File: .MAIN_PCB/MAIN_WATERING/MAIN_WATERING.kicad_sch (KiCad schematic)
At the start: 5 parts, among them J1 Conn_01x04_Pin, SW1 SW_Push, U1 XIAO-ESP32-C3-SMD

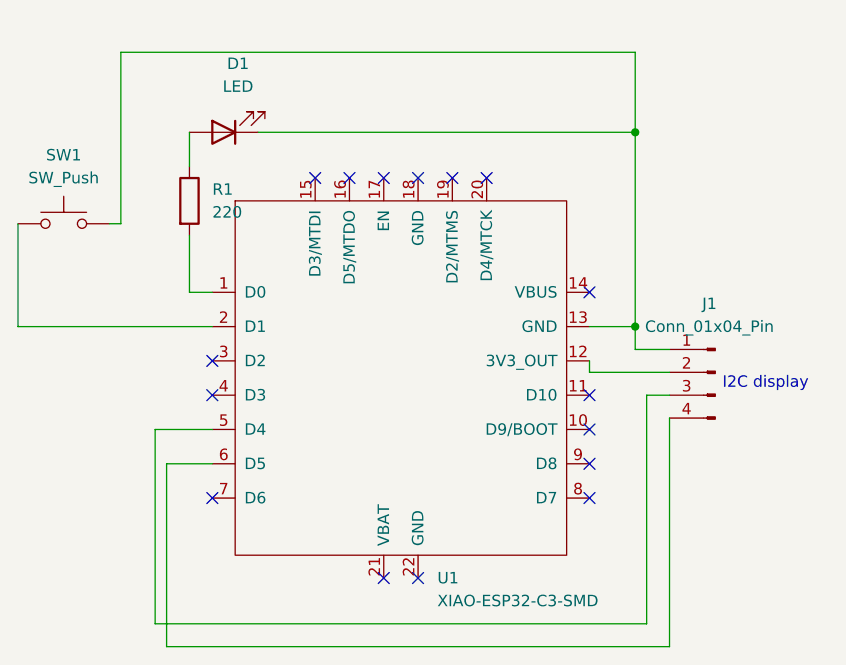
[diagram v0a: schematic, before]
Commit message: fixed ESP drawing in the wiring diagram
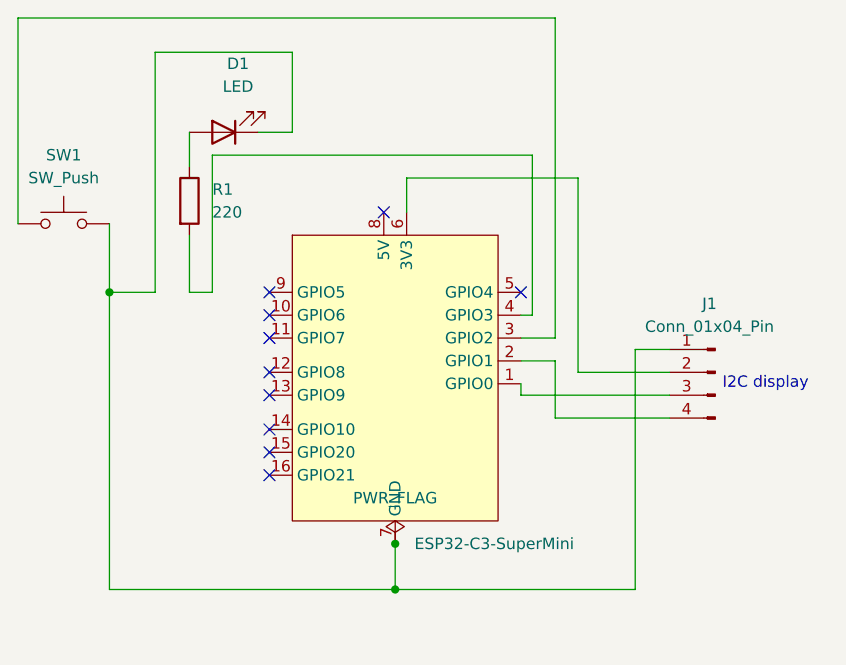
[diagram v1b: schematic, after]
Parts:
- removed U1: XIAO-ESP32-C3-SMD, kicadplugnis:ESP32-C3-SuperMini, symbol Seeed_Studio_XIAO_Series:XIAO-ESP32-C3-SMD
- added U1: ESP32-C3-SuperMini, kicadplugnis:ESP32-C3-SuperMini, symbol ESP32-C3-SuperMini:ESP32-C3-SuperMini
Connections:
- net at D1.1 (K), J1.1 (Pin_1), SW1.2: now also U1.7 (GND)
- net at J1.2 (Pin_2): now also U1.6 (3V3)
- net at J1.3 (Pin_3): now also U1.1 (GPIO0)
- net at J1.4 (Pin_4): now also U1.2 (GPIO1)
- net at R1.2: now also U1.4 (GPIO3)
- net at SW1.1: now also U1.3 (GPIO2)
- no-connect marks 16 -> 10
